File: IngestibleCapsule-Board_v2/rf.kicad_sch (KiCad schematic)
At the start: 17 parts, among them J6 Conn_01x02_Pin, U5 SR1010, Y3 ABS07

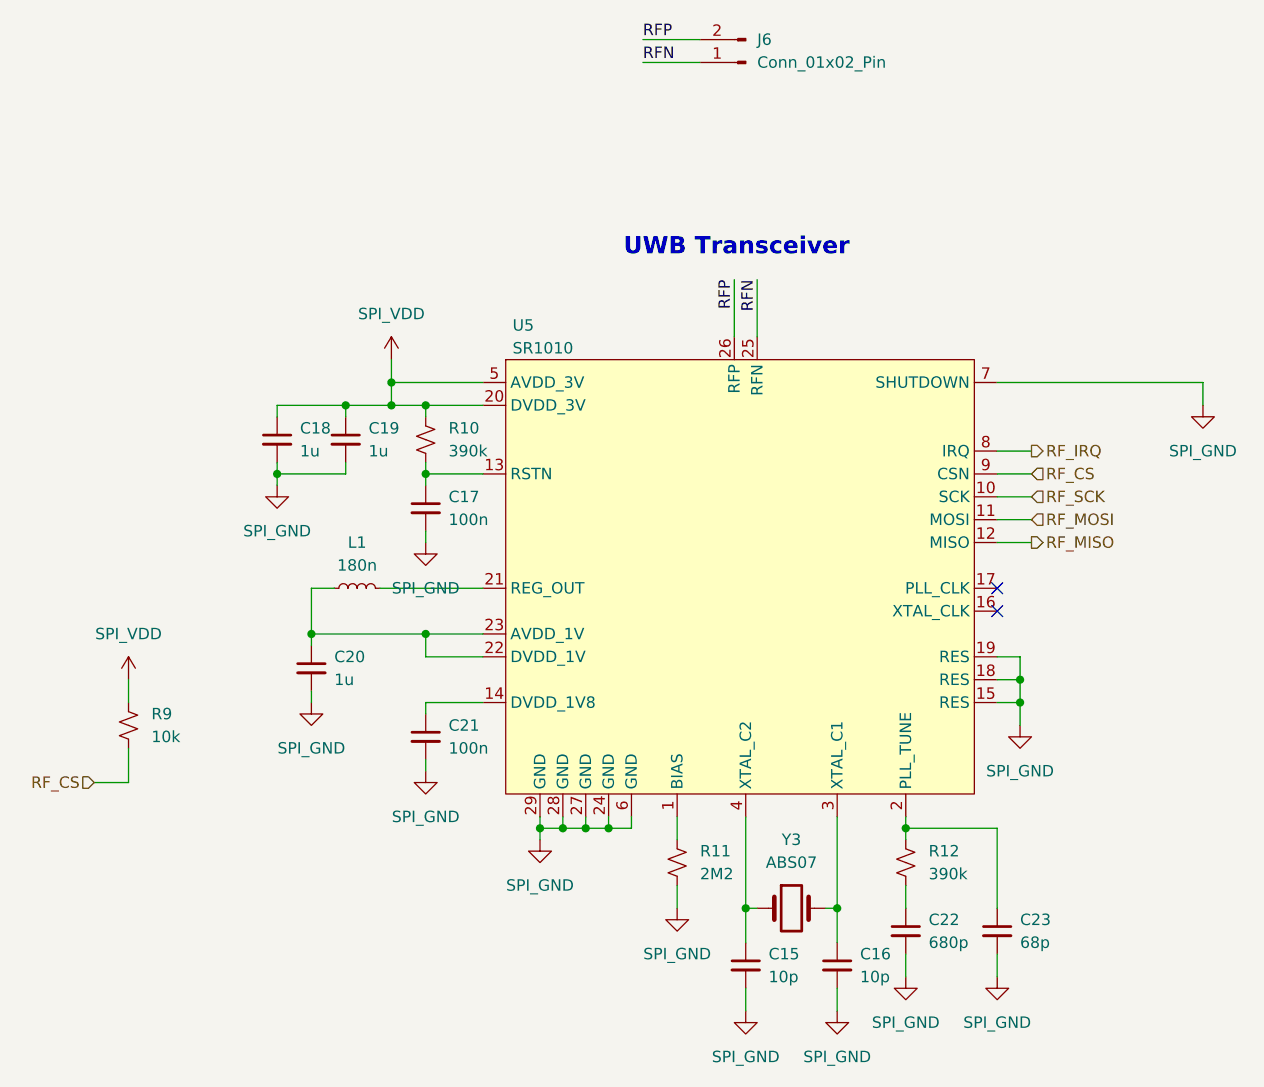
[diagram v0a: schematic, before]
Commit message: full v2 implementation, has 5 circles connected by mousebites
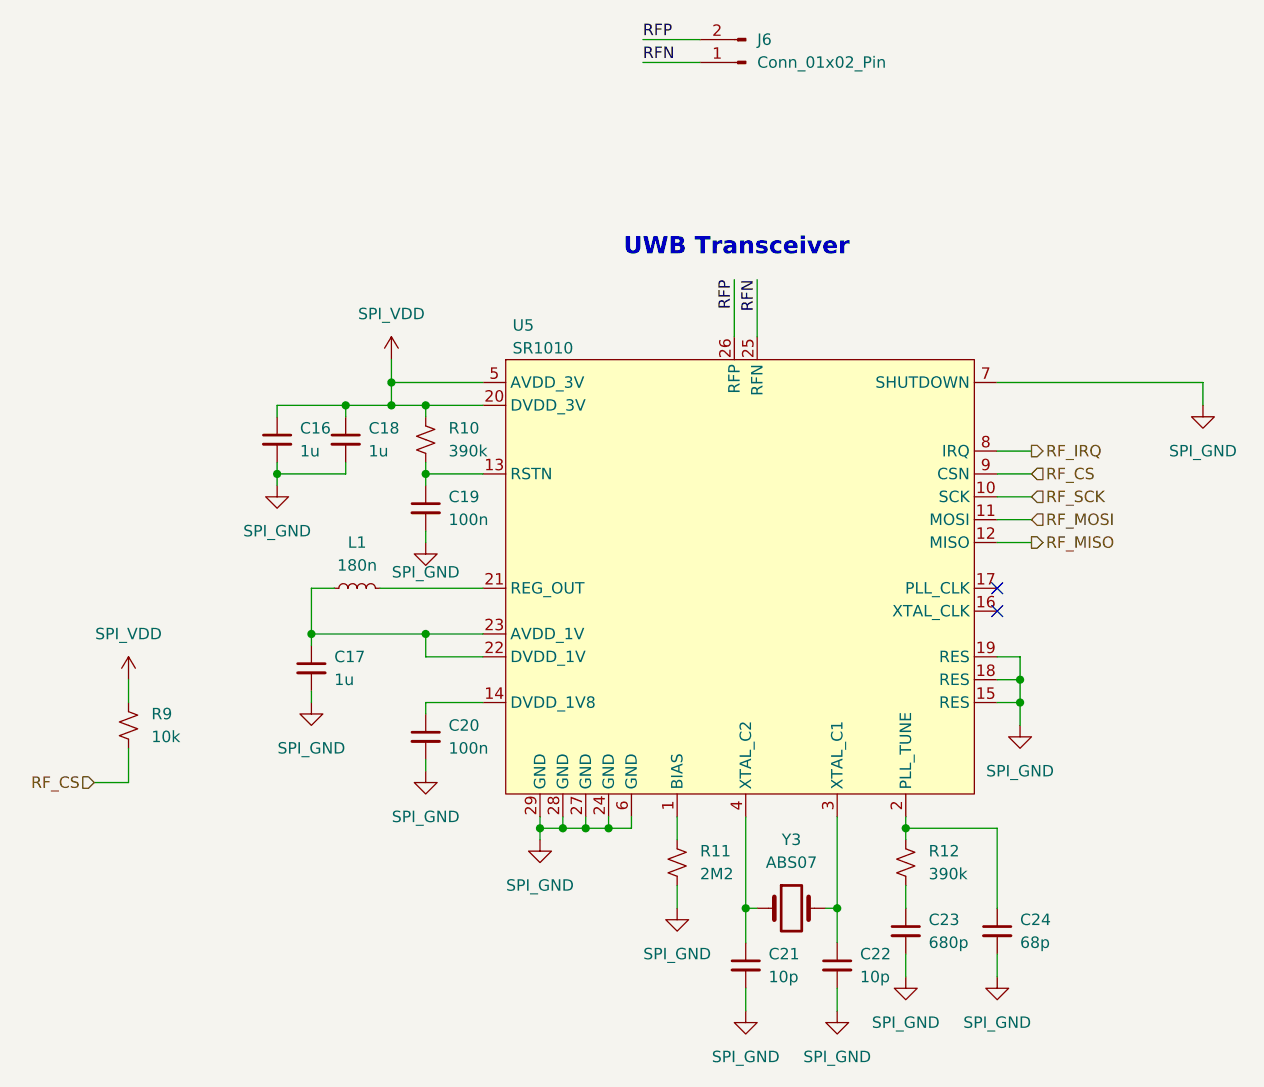
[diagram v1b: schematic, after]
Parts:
- U5: footprint Package_DFN_QFN:QFN-28-1EP_4x4mm_P0.4mm_EP2.7x2.7mm -> kjp_fplib:SR1010
- renumbered C18 to C16, C20 to C17, C19 to C18, C17 to C19, C21 to C20, C15 to C21, C16 to C22, C22 to C23, C23 to C24
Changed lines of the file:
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@@
 		(dnp no)
 		(fields_autoplaced yes)
-		(property "Reference" "#PWR078"
+		(property "Reference" "#PWR054"
 			(at 87.63 96.52 0)
 			(effects
@@
 			(project "IngestibleCapsule-Board"
 				(path "/c8668ce4-f244-4f6b-86d5-e45f0742e988/1d174589-7caa-4bd8-831f-7b0bb033a2b0"
-					(reference "#PWR078")
+					(reference "#PWR054")
 					(unit 1)
 				)
@@
 		(dnp no)
 		(fields_autoplaced yes)
-		(property "Reference" "C15"
+		(property "Reference" "C21"
 			(at 142.24 142.2462 0)
 			(effects
@@
 			(project ""
 				(path "/c8668ce4-f244-4f6b-86d5-e45f0742e988/1d174589-7caa-4bd8-831f-7b0bb033a2b0"
-					(reference "C15")
+					(reference "C21")
 					(unit 1)
 				)
@@
 		(dnp no)
 		(fields_autoplaced yes)
-		(property "Reference" "#PWR089"
+		(property "Reference" "#PWR066"
 			(at 190.5 87.63 0)
 			(effects
@@
 			(project "IngestibleCapsule-Board"
 				(path "/c8668ce4-f244-4f6b-86d5-e45f0742e988/1d174589-7caa-4bd8-831f-7b0bb033a2b0"
-					(reference "#PWR089")
+					(reference "#PWR066")
 					(unit 1)
 				)
@@
 		(dnp no)
 		(fields_autoplaced yes)
-		(property "Reference" "C16"
+		(property "Reference" "C22"
 			(at 152.4 142.2462 0)
 			(effects
@@
 			(project "IngestibleCapsule-Board"
 				(path "/c8668ce4-f244-4f6b-86d5-e45f0742e988/1d174589-7caa-4bd8-831f-7b0bb033a2b0"
-					(reference "C16")
+					(reference "C22")
 					(unit 1)
 				)
@@
 		(dnp no)
 		(fields_autoplaced yes)
-		(property "Reference" "#PWR085"
+		(property "Reference" "#PWR062"
 			(at 149.86 154.94 0)
 			(effects
@@
 			(project "IngestibleCapsule-Board"
 				(path "/c8668ce4-f244-4f6b-86d5-e45f0742e988/1d174589-7caa-4bd8-831f-7b0bb033a2b0"
-					(reference "#PWR085")
+					(reference "#PWR062")
 					(unit 1)
 				)
@@
 		(dnp no)
 		(fields_autoplaced yes)
-		(property "Reference" "#PWR086"
+		(property "Reference" "#PWR063"
 			(at 157.48 151.13 0)
 			(effects
@@
 			(project "IngestibleCapsule-Board"
 				(path "/c8668ce4-f244-4f6b-86d5-e45f0742e988/1d174589-7caa-4bd8-831f-7b0bb033a2b0"
-					(reference "#PWR086")
+					(reference "#PWR063")
 					(unit 1)
 				)
@@
 		(dnp no)
 		(fields_autoplaced yes)
-		(property "Reference" "C19"
+		(property "Reference" "C18"
 			(at 97.79 83.8262 0)
 			(effects
@@
 			(project "IngestibleCapsule-Board"
 				(path "/c8668ce4-f244-4f6b-86d5-e45f0742e988/1d174589-7caa-4bd8-831f-7b0bb033a2b0"
-					(reference "C19")
+					(reference "C18")
 					(unit 1)
 				)
@@
 		(dnp no)
 		(fields_autoplaced yes)
-		(property "Reference" "#PWR077"
+		(property "Reference" "#PWR056"
 			(at 100.33 80.01 0)
 			(effects
@@
 			(project "IngestibleCapsule-Board"
 				(path "/c8668ce4-f244-4f6b-86d5-e45f0742e988/1d174589-7caa-4bd8-831f-7b0bb033a2b0"
-					(reference "#PWR077")
+					(reference "#PWR056")
 					(unit 1)
 				)
@@
 		(dnp no)
 		(fields_autoplaced yes)
-		(property "Reference" "C23"
+		(property "Reference" "C24"
 			(at 170.18 138.4362 0)
 			(effects
@@
 			(project "IngestibleCapsule-Board"
 				(path "/c8668ce4-f244-4f6b-86d5-e45f0742e988/1d174589-7caa-4bd8-831f-7b0bb033a2b0"
-					(reference "C23")
+					(reference "C24")
 					(unit 1)
 				)
@@
 		(dnp no)
 		(fields_autoplaced yes)
-		(property "Reference" "#PWR082"
+		(property "Reference" "#PWR059"
 			(at 116.84 135.89 0)
 			(effects
@@
 			(project "IngestibleCapsule-Board"
 				(path "/c8668ce4-f244-4f6b-86d5-e45f0742e988/1d174589-7caa-4bd8-831f-7b0bb033a2b0"
-					(reference "#PWR082")
+					(reference "#PWR059")
 					(unit 1)
 				)
@@
 		(dnp no)
 		(fields_autoplaced yes)
-		(property "Reference" "#PWR088"
+		(property "Reference" "#PWR065"
 			(at 170.18 123.19 0)
 			(effects
@@
 			(project "IngestibleCapsule-Board"
 				(path "/c8668ce4-f244-4f6b-86d5-e45f0742e988/1d174589-7caa-4bd8-831f-7b0bb033a2b0"
-					(reference "#PWR088")
+					(reference "#PWR065")
 					(unit 1)
 				)
@@
 		(dnp no)
 		(fields_autoplaced yes)
-		(property "Reference" "#PWR083"
+		(property "Reference" "#PWR060"
 			(at 132.08 143.51 0)
 			(effects
@@
 			(project "IngestibleCapsule-Board"
 				(path "/c8668ce4-f244-4f6b-86d5-e45f0742e988/1d174589-7caa-4bd8-831f-7b0bb033a2b0"
-					(reference "#PWR083")
+					(reference "#PWR060")
 					(unit 1)
 				)
@@
 		(dnp no)
 		(fields_autoplaced yes)
-		(property "Reference" "C21"
+		(property "Reference" "C20"
 			(at 106.68 116.8462 0)
 			(effects
@@
 			(project "IngestibleCapsule-Board"
 				(path "/c8668ce4-f244-4f6b-86d5-e45f0742e988/1d174589-7caa-4bd8-831f-7b0bb033a2b0"
-					(reference "C21")
+					(reference "C20")
 					(unit 1)
 				)
@@
 		(dnp no)
 		(fields_autoplaced yes)
-		(property "Reference" "C20"
+		(property "Reference" "C17"
 			(at 93.98 109.2262 0)
 			(effects
@@
 			(project "IngestibleCapsule-Board"
 				(path "/c8668ce4-f244-4f6b-86d5-e45f0742e988/1d174589-7caa-4bd8-831f-7b0bb033a2b0"
-					(reference "C20")
+					(reference "C17")
 					(unit 1)
 				)
@@
 		(dnp no)
 		(fields_autoplaced yes)
-		(property "Reference" "#PWR081"
+		(property "Reference" "#PWR058"
 			(at 104.14 128.27 0)
 			(effects
@@
 			(project "IngestibleCapsule-Board"
 				(path "/c8668ce4-f244-4f6b-86d5-e45f0742e988/1d174589-7caa-4bd8-831f-7b0bb033a2b0"
-					(reference "#PWR081")
+					(reference "#PWR058")
 					(unit 1)
 				)
@@
 		(dnp no)
 		(fields_autoplaced yes)
-		(property "Reference" "#PWR076"
+		(property "Reference" "#PWR053"
 			(at 71.12 115.57 0)
 			(effects
@@
 			(project "IngestibleCapsule-Board"
 				(path "/c8668ce4-f244-4f6b-86d5-e45f0742e988/1d174589-7caa-4bd8-831f-7b0bb033a2b0"
-					(reference "#PWR076")
+					(reference "#PWR053")
 					(unit 1)
 				)
@@
 		(dnp no)
 		(fields_autoplaced yes)
-		(property "Reference" "#PWR084"
+		(property "Reference" "#PWR061"
 			(at 139.7 154.94 0)
 			(effects
@@
 			(project "IngestibleCapsule-Board"
 				(path "/c8668ce4-f244-4f6b-86d5-e45f0742e988/1d174589-7caa-4bd8-831f-7b0bb033a2b0"
-					(reference "#PWR084")
+					(reference "#PWR061")
 					(unit 1)
 				)
@@
 		(dnp no)
 		(fields_autoplaced yes)
-		(property "Reference" "#PWR080"
+		(property "Reference" "#PWR055"
 			(at 91.44 120.65 0)
 			(effects
@@
 			(project "IngestibleCapsule-Board"
 				(path "/c8668ce4-f244-4f6b-86d5-e45f0742e988/1d174589-7caa-4bd8-831f-7b0bb033a2b0"
-					(reference "#PWR080")
+					(reference "#PWR055")
 					(unit 1)
 				)
@@
 			)
 		)
-		(property "Footprint" "Package_DFN_QFN:QFN-28-1EP_4x4mm_P0.4mm_EP2.7x2.7mm"
+		(property "Footprint" "kjp_fplib:SR1010"
 			(at 139.7 92.71 0)
 			(effects
@@
 		(dnp no)
 		(fields_autoplaced yes)
-		(property "Reference" "C17"
+		(property "Reference" "C19"
 			(at 106.68 91.4462 0)
 			(effects
@@
 			(project ""
 				(path "/c8668ce4-f244-4f6b-86d5-e45f0742e988/1d174589-7caa-4bd8-831f-7b0bb033a2b0"
-					(reference "C17")
+					(reference "C19")
 					(unit 1)
 				)
@@
 		(dnp no)
 		(fields_autoplaced yes)
-		(property "Reference" "C18"
+		(property "Reference" "C16"
 			(at 90.17 83.8262 0)
 			(effects
@@
 			(project "IngestibleCapsule-Board"
 				(path "/c8668ce4-f244-4f6b-86d5-e45f0742e988/1d174589-7caa-4bd8-831f-7b0bb033a2b0"
-					(reference "C18")
+					(reference "C16")
 					(unit 1)
 				)
@@
 		(dnp no)
 		(fields_autoplaced yes)
-		(property "Reference" "#PWR087"
+		(property "Reference" "#PWR064"
 			(at 167.64 151.13 0)
 			(effects
@@
 			(project "IngestibleCapsule-Board"
 				(path "/c8668ce4-f244-4f6b-86d5-e45f0742e988/1d174589-7caa-4bd8-831f-7b0bb033a2b0"
-					(reference "#PWR087")
+					(reference "#PWR064")
 					(unit 1)
 				)
@@
 		(dnp no)
 		(fields_autoplaced yes)
-		(property "Reference" "C22"
+		(property "Reference" "C23"
 			(at 160.02 138.4362 0)
 			(effects
@@
 			(project "IngestibleCapsule-Board"
 				(path "/c8668ce4-f244-4f6b-86d5-e45f0742e988/1d174589-7caa-4bd8-831f-7b0bb033a2b0"
-					(reference "C22")
+					(reference "C23")
 					(unit 1)
 				)
@@
 		(on_board yes)
 		(dnp no)
-		(fields_autoplaced yes)
-		(property "Reference" "#PWR079"
+		(property "Reference" "#PWR057"
 			(at 104.14 102.87 0)
 			(effects
@@
 		)
 		(property "Value" "SPI_GND"
-			(at 104.14 101.6 0)
+			(at 104.14 99.822 0)
 			(effects
 				(font
@@
 			(project "IngestibleCapsule-Board"
 				(path "/c8668ce4-f244-4f6b-86d5-e45f0742e988/1d174589-7caa-4bd8-831f-7b0bb033a2b0"
-					(reference "#PWR079")
-					(unit 1)
-				)
+					(reference "#PWR057")
+					(unit 1)
+				)
